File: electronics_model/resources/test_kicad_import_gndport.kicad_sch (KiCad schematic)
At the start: 3 parts

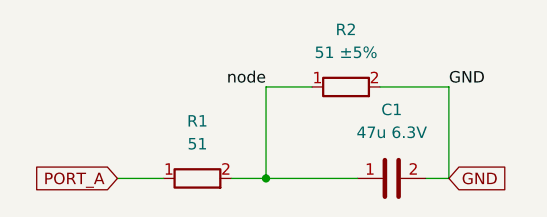
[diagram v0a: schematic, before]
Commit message: fix overlapped port name test
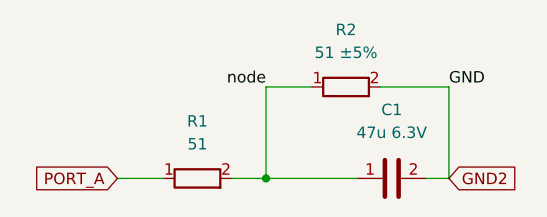
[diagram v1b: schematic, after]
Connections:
- net GND renamed GND2
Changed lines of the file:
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@@
     )
   )
-  (global_label "GND" (shape input) (at 111.76 96.52 0) (fields_autoplaced)
+  (global_label "GND2" (shape input) (at 111.76 96.52 0) (fields_autoplaced)
     (effects (font (size 1.27 1.27)) (justify left))
-    (property "Intersheet References" "${INTERSHEET_REFS}" (id 0) (at 118.0436 96.4406 0)
+    (property "Intersheet References" "${INTERSHEET_REFS}" (id 0) (at 119.2531 96.4406 0)
       (effects (font (size 1.27 1.27)) (justify left) hide)
     )
